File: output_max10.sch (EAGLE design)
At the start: 66 parts, among them IC4 IS61WV1288EEBLL-10HLI, IC5 10M04EQFP144, Q1 25MHz

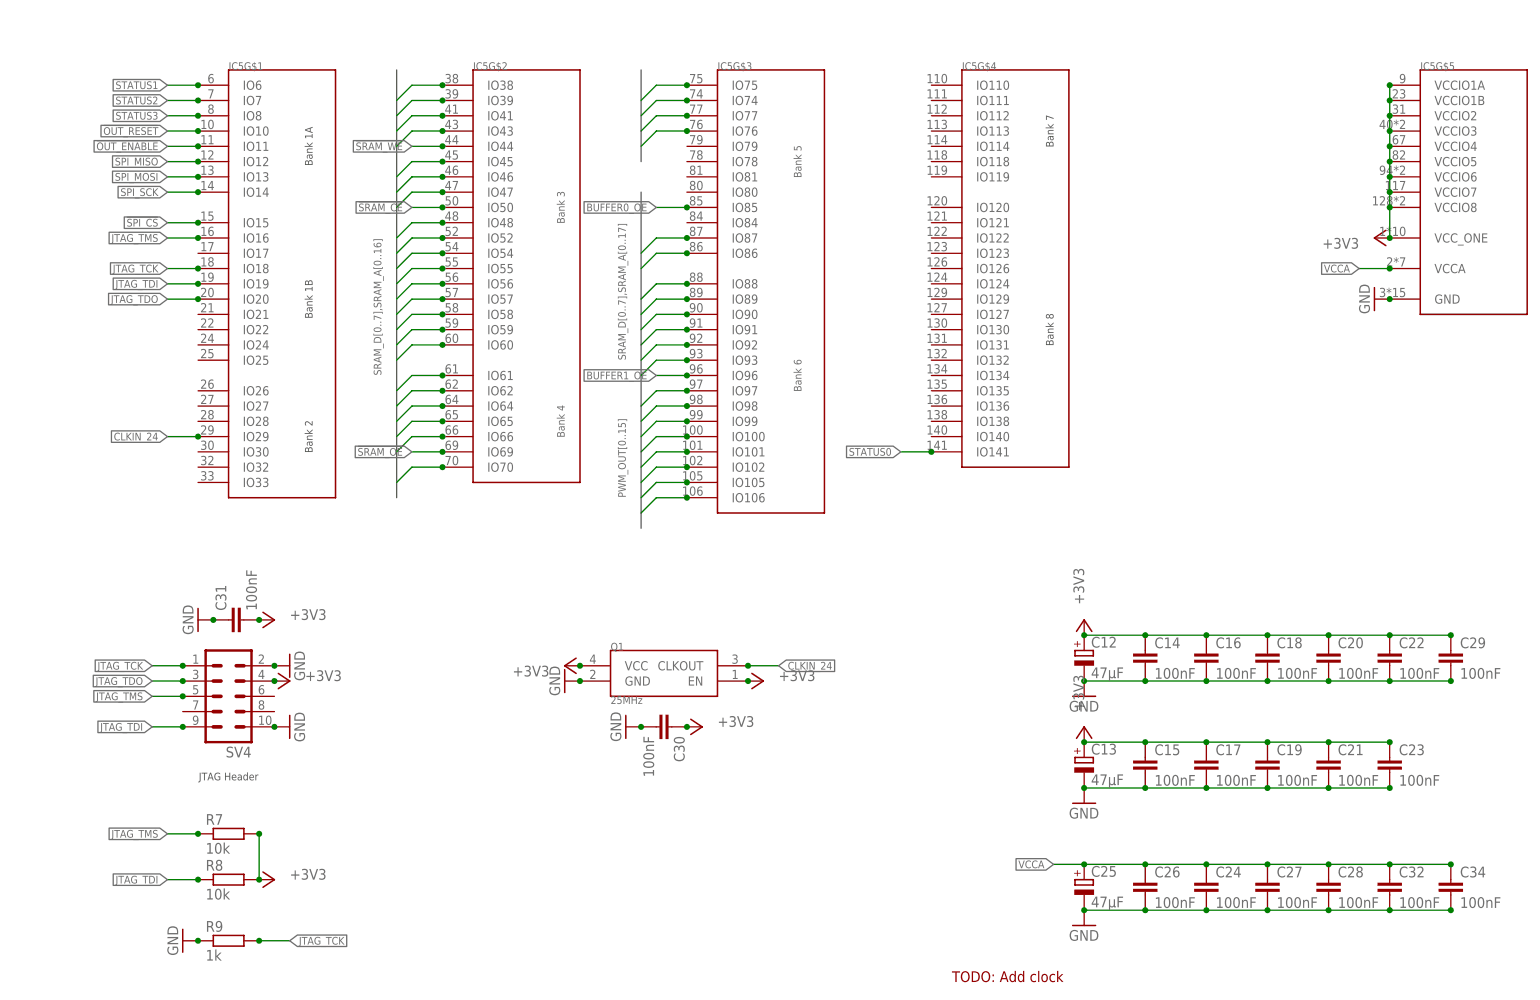
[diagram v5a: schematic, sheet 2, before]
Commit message: Added some required reisstors to FPGA outputboard
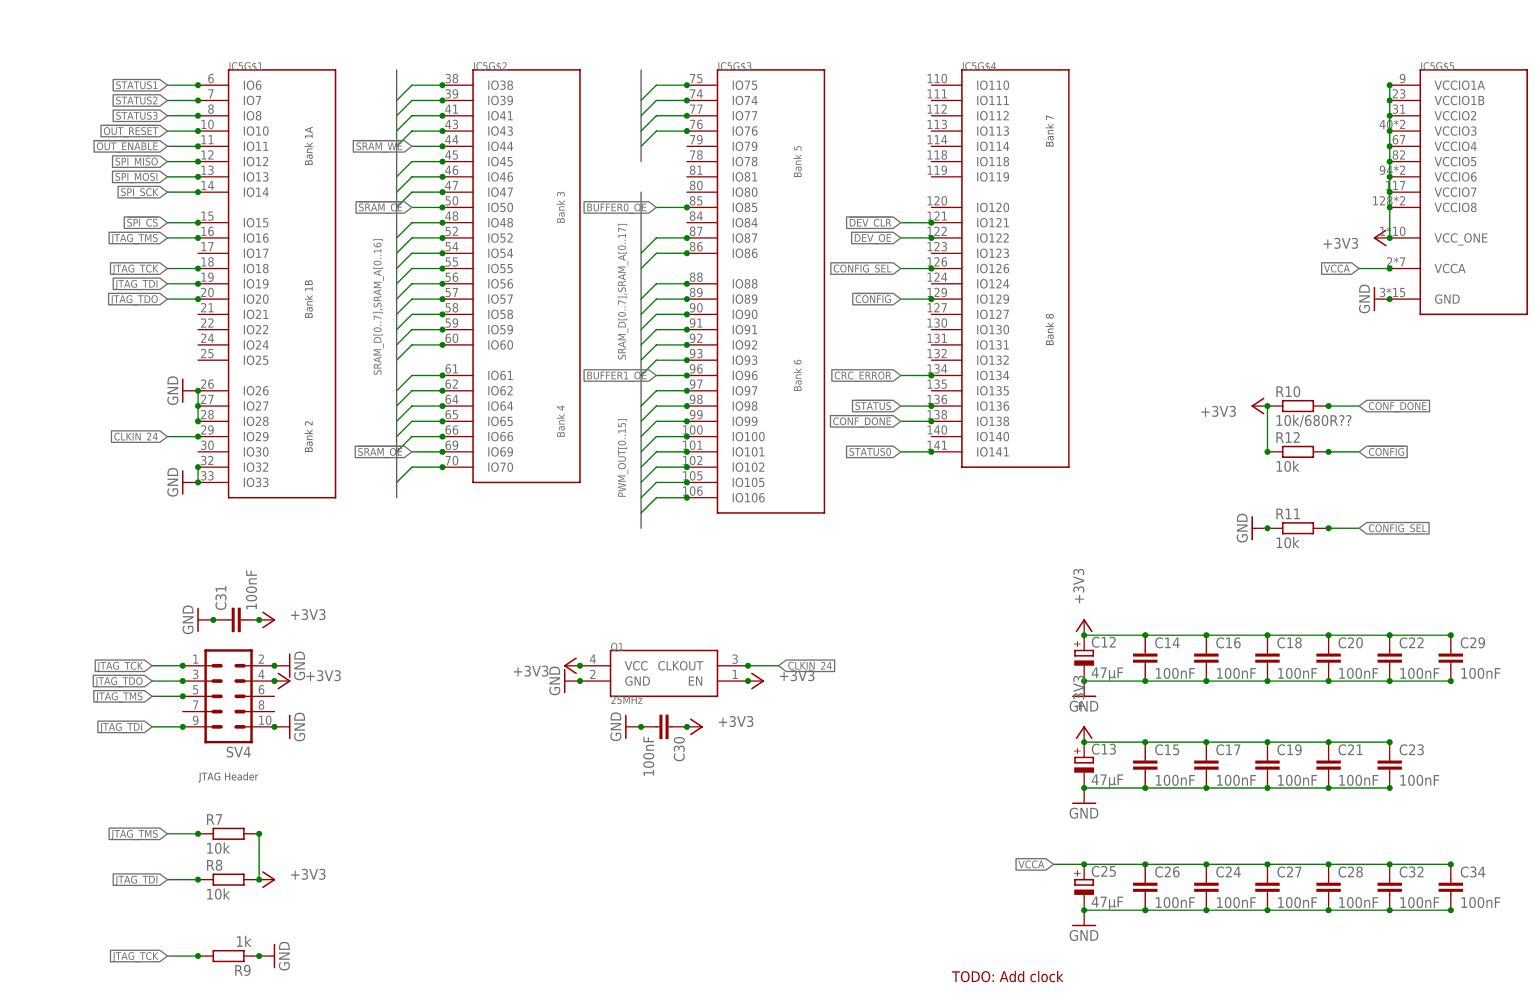
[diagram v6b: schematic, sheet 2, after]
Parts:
- added LED6: (no value), led:LEDCHIPLED_1206
- added R10: 10k/680R??, rcl:R-EU_M0805
- added R11, R12: 10k, rcl:R-EU_M0805
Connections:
- new net !CONFIG: IC5G$4.IO129, R12.2
- new net !DEV_CLR: IC5G$4.IO121
- new net !STATUS: IC5G$4.IO136
- new net CONFIG_SEL: IC5G$4.IO126, R11.2
- new net CONF_DONE: IC5G$4.IO138, LED6.A, R10.2
- new net CRC_ERROR: IC5G$4.IO134
- new net DEV_OE: IC5G$4.IO122
- net +3V3: now also R10.1, R12.1
- net GND: now also IC5G$1.IO26, IC5G$1.IO27, IC5G$1.IO28, IC5G$1.IO32, IC5G$1.IO33, LED6.C, R11.1
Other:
- moved on the sheet: R9
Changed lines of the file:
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@@
 <attribute name="MOUSER" value="710-885012207072"/>
 </part>
+<part name="R10" library="rcl" library_urn="urn:adsk.eagle:library:334" deviceset="R-EU_" device="M0805" package3d_urn="urn:adsk.eagle:package:23556/1" value="10k/680R??">
+<attribute name="MOUSER" value="652-CR0805FX-1002ELF"/>
+</part>
+<part name="+3V10" library="supply1" library_urn="urn:adsk.eagle:library:371" deviceset="+3V3" device=""/>
+<part name="LED6" library="led" library_urn="urn:adsk.eagle:library:259" deviceset="LED" device="CHIPLED_1206" package3d_urn="urn:adsk.eagle:package:15823/2">
+<attribute name="MOUSER" value="604-APTR3216SGC"/>
+</part>
+<part name="R11" library="rcl" library_urn="urn:adsk.eagle:library:334" deviceset="R-EU_" device="M0805" package3d_urn="urn:adsk.eagle:package:23556/1" value="10k">
+<attribute name="MOUSER" value="652-CR0805FX-1002ELF"/>
+</part>
+<part name="GND26" library="supply1" library_urn="urn:adsk.eagle:library:371" deviceset="GND" device=""/>
+<part name="R12" library="rcl" library_urn="urn:adsk.eagle:library:334" deviceset="R-EU_" device="M0805" package3d_urn="urn:adsk.eagle:package:23556/1" value="10k">
+<attribute name="MOUSER" value="652-CR0805FX-1002ELF"/>
+</part>
+<part name="GND27" library="supply1" library_urn="urn:adsk.eagle:library:371" deviceset="GND" device=""/>
+<part name="GND28" library="supply1" library_urn="urn:adsk.eagle:library:371" deviceset="GND" device=""/>
 </parts>
 <sheets>
@@
 <instance part="+3V9" gate="G$1" x="109.22" y="66.04" smashed="yes">
 <attribute name="VALUE" x="109.22" y="66.04" size="1.778" layer="96"/>
+</instance>
+<instance part="LED6" gate="G$1" x="231.14" y="139.7" rot="R90">
+<attribute name="MOUSER" x="231.14" y="139.7" size="1.27" layer="96" rot="R90" align="top-center" display="off"/>
 </instance>
 </instances>
@@
 <wire x1="236.22" y1="154.94" x2="236.22" y2="147.32" width="0.1524" layer="91"/>
 <junction x="236.22" y="147.32"/>
+<pinref part="LED6" gate="G$1" pin="C"/>
+<wire x1="236.22" y1="139.7" x2="236.22" y2="147.32" width="0.1524" layer="91"/>
+<junction x="236.22" y="139.7"/>
 </segment>
 <segment>
@@
 <label x="33.02" y="12.7" size="1.27" layer="95" rot="R270" xref="yes"/>
 <junction x="33.02" y="20.32"/>
+</segment>
+</net>
+<net name="CONF_DONE" class="0">
+<segment>
+<pinref part="LED6" gate="G$1" pin="A"/>
+<wire x1="228.6" y1="139.7" x2="213.36" y2="139.7" width="0.1524" layer="91"/>
+<label x="213.36" y="139.7" size="1.27" layer="95" rot="R180" xref="yes"/>
+<junction x="228.6" y="139.7"/>
 </segment>
 </net>
@@
 <attribute name="MOUSER" x="30.48" y="48.26" size="1.27" layer="96" align="top-center" display="off"/>
 </instance>
-<instance part="R9" gate="G$1" x="30.48" y="38.1">
-<attribute name="MOUSER" x="30.48" y="38.1" size="1.27" layer="96" align="top-center" display="off"/>
-</instance>
-<instance part="GND19" gate="1" x="22.86" y="38.1" rot="R270"/>
+<instance part="R9" gate="G$1" x="30.48" y="35.56" rot="R180">
+<attribute name="MOUSER" x="30.48" y="35.56" size="1.27" layer="96" rot="R180" align="top-center" display="off"/>
+</instance>
+<instance part="GND19" gate="1" x="38.1" y="35.56" rot="R90"/>
 <instance part="+3V2" gate="G$1" x="38.1" y="48.26" smashed="yes" rot="R270">
 <attribute name="VALUE" x="40.64" y="48.26" size="1.778" layer="96"/>
@@
 <attribute name="MOUSER" x="233.68" y="48.26" size="1.27" layer="96" align="top-center" display="off"/>
 </instance>
+<instance part="R10" gate="G$1" x="208.28" y="127">
+<attribute name="MOUSER" x="208.28" y="127" size="1.27" layer="96" align="top-center" display="off"/>
+</instance>
+<instance part="+3V10" gate="G$1" x="200.66" y="127" smashed="yes" rot="R90">
+<attribute name="VALUE" x="198.12" y="127" size="1.778" layer="96" rot="R180"/>
+</instance>
+<instance part="R11" gate="G$1" x="208.28" y="106.68">
+<attribute name="MOUSER" x="208.28" y="106.68" size="1.27" layer="96" align="top-center" display="off"/>
+</instance>
+<instance part="GND26" gate="1" x="200.66" y="106.68" rot="R270"/>
+<instance part="R12" gate="G$1" x="208.28" y="119.38">
+<attribute name="MOUSER" x="208.28" y="119.38" size="1.27" layer="96" align="top-center" display="off"/>
+</instance>
+<instance part="GND27" gate="1" x="22.86" y="129.54" rot="R270"/>
+<instance part="GND28" gate="1" x="22.86" y="114.3" rot="R270"/>
 </instances>
 <busses>
@@
 <junction x="35.56" y="91.44"/>
 </segment>
+<segment>
+<pinref part="R10" gate="G$1" pin="1"/>
+<pinref part="+3V10" gate="G$1" pin="+3V3"/>
+<junction x="203.2" y="127"/>
+<pinref part="R12" gate="G$1" pin="1"/>
+<wire x1="203.2" y1="127" x2="203.2" y2="119.38" width="0.1524" layer="91"/>
+<junction x="203.2" y="119.38"/>
+</segment>
 </net>
 <net name="GND" class="0">
@@
 <pinref part="R9" gate="G$1" pin="1"/>
 <pinref part="GND19" gate="1" pin="GND"/>
-<junction x="25.4" y="38.1"/>
+<junction x="35.56" y="35.56"/>
 </segment>
 <segment>
@@
 <junction x="27.94" y="91.44"/>
 </segment>
+<segment>
+<pinref part="R11" gate="G$1" pin="1"/>
+<pinref part="GND26" gate="1" pin="GND"/>
+<junction x="203.2" y="106.68"/>
+</segment>
+<segment>
+<pinref part="IC5" gate="G$1" pin="IO26"/>
+<pinref part="IC5" gate="G$1" pin="IO28"/>
+<wire x1="25.4" y1="129.54" x2="25.4" y2="127" width="0.1524" layer="91"/>
+<junction x="25.4" y="129.54"/>
+<pinref part="IC5" gate="G$1" pin="IO27"/>
+<junction x="25.4" y="127"/>
+<wire x1="25.4" y1="127" x2="25.4" y2="124.46" width="0.1524" layer="91"/>
+<junction x="25.4" y="124.46"/>
+<pinref part="GND27" gate="1" pin="GND"/>
+</segment>
+<segment>
+<pinref part="IC5" gate="G$1" pin="IO32"/>
+<pinref part="IC5" gate="G$1" pin="IO33"/>
+<wire x1="25.4" y1="116.84" x2="25.4" y2="114.3" width="0.1524" layer="91"/>
+<junction x="25.4" y="116.84"/>
+<junction x="25.4" y="114.3"/>
+<pinref part="GND28" gate="1" pin="GND"/>
+</segment>
 </net>
 <net name="JTAG_TMS" class="0">
@@
 <segment>
 <pinref part="R9" gate="G$1" pin="2"/>
-<wire x1="35.56" y1="38.1" x2="40.64" y2="38.1" width="0.1524" layer="91"/>
-<label x="40.64" y="38.1" size="1.27" layer="95" xref="yes"/>
-<junction x="35.56" y="38.1"/>
+<wire x1="25.4" y1="35.56" x2="20.32" y2="35.56" width="0.1524" layer="91"/>
+<label x="20.32" y="35.56" size="1.27" layer="95" rot="R180" xref="yes"/>
+<junction x="25.4" y="35.56"/>
 </segment>
 </net>
@@
 </segment>
 </net>
+<net name="CONF_DONE" class="0">
+<segment>
+<pinref part="IC5" gate="G$4" pin="IO138"/>
+<wire x1="147.32" y1="124.46" x2="142.24" y2="124.46" width="0.1524" layer="91"/>
+<label x="142.24" y="124.46" size="1.27" layer="95" rot="R180" xref="yes"/>
+<junction x="147.32" y="124.46"/>
+</segment>
+<segment>
+<pinref part="R10" gate="G$1" pin="2"/>
+<wire x1="213.36" y1="127" x2="218.44" y2="127" width="0.1524" layer="91"/>
+<label x="218.44" y="127" size="1.27" layer="95" xref="yes"/>
+<junction x="213.36" y="127"/>
+</segment>
+</net>
+<net name="!STATUS" class="0">
+<segment>
+<pinref part="IC5" gate="G$4" pin="IO136"/>
+<wire x1="147.32" y1="127" x2="142.24" y2="127" width="0.1524" layer="91"/>
+<label x="142.24" y="127" size="1.27" layer="95" rot="R180" xref="yes"/>
+<junction x="147.32" y="127"/>
+</segment>
+</net>
+<net name="CONFIG_SEL" class="0">
+<segment>
+<pinref part="IC5" gate="G$4" pin="IO126"/>
+<wire x1="147.32" y1="149.86" x2="142.24" y2="149.86" width="0.1524" layer="91"/>
+<label x="142.24" y="149.86" size="1.27" layer="95" rot="R180" xref="yes"/>
+<junction x="147.32" y="149.86"/>
+</segment>
+<segment>
+<pinref part="R11" gate="G$1" pin="2"/>
+<wire x1="213.36" y1="106.68" x2="218.44" y2="106.68" width="0.1524" layer="91"/>
+<label x="218.44" y="106.68" size="1.27" layer="95" xref="yes"/>
+<junction x="213.36" y="106.68"/>
+</segment>
+</net>
+<net name="CRC_ERROR" class="0">
+<segment>
+<pinref part="IC5" gate="G$4" pin="IO134"/>
+<wire x1="147.32" y1="132.08" x2="142.24" y2="132.08" width="0.1524" layer="91"/>
+<label x="142.24" y="132.08" size="1.27" layer="95" rot="R180" xref="yes"/>
+<junction x="147.32" y="132.08"/>
+</segment>
+</net>
+<net name="DEV_OE" class="0">
+<segment>
+<pinref part="IC5" gate="G$4" pin="IO122"/>
+<wire x1="147.32" y1="154.94" x2="142.24" y2="154.94" width="0.1524" layer="91"/>
+<label x="142.24" y="154.94" size="1.27" layer="95" rot="R180" xref="yes"/>
+<junction x="147.32" y="154.94"/>
+</segment>
+</net>
+<net name="!DEV_CLR" class="0">
+<segment>
+<pinref part="IC5" gate="G$4" pin="IO121"/>
+<wire x1="147.32" y1="157.48" x2="142.24" y2="157.48" width="0.1524" layer="91"/>
+<label x="142.24" y="157.48" size="1.27" layer="95" rot="R180" xref="yes"/>
+<junction x="147.32" y="157.48"/>
+</segment>
+</net>
+<net name="!CONFIG" class="0">
+<segment>
+<pinref part="IC5" gate="G$4" pin="IO129"/>
+<wire x1="147.32" y1="144.78" x2="142.24" y2="144.78" width="0.1524" layer="91"/>
+<label x="142.24" y="144.78" size="1.27" layer="95" rot="R180" xref="yes"/>
+<junction x="147.32" y="144.78"/>
+</segment>
+<segment>
+<pinref part="R12" gate="G$1" pin="2"/>
+<wire x1="213.36" y1="119.38" x2="218.44" y2="119.38" width="0.1524" layer="91"/>
+<label x="218.44" y="119.38" size="1.27" layer="95" xref="yes"/>
+<junction x="213.36" y="119.38"/>
+</segment>
+</net>

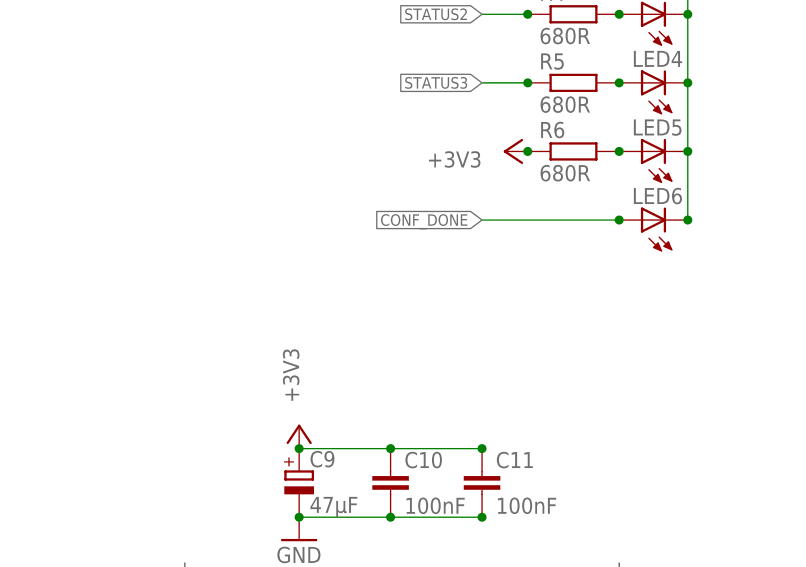
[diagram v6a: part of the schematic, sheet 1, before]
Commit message: Minor component placemnet changes for MAX10 output board to fix mechanical issues
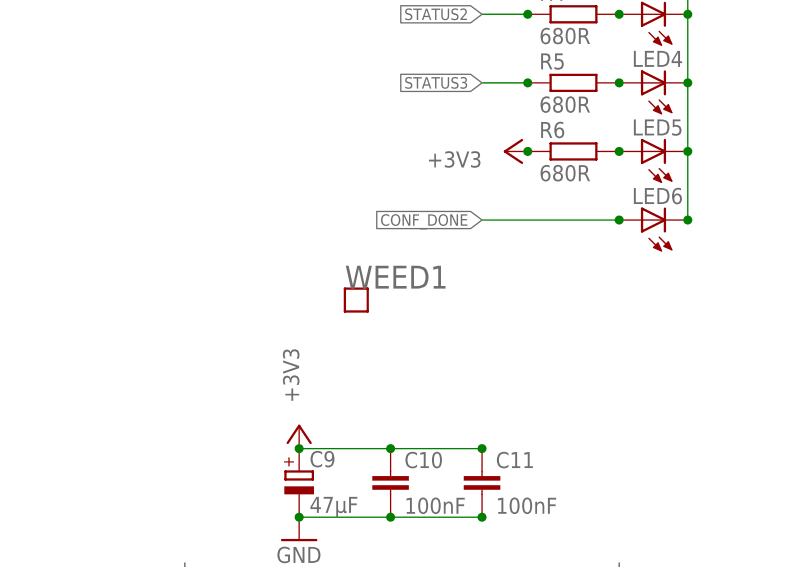
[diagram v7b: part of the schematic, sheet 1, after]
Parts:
- added WEED1: WEED, lichtenstein_onion:WEED
- R10: value 10k/680R?? -> 10k
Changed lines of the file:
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@@
 <attribute name="MOUSER" value="710-885012207072"/>
 </part>
-<part name="R10" library="rcl" library_urn="urn:adsk.eagle:library:334" deviceset="R-EU_" device="M0805" package3d_urn="urn:adsk.eagle:package:23556/1" value="10k/680R??">
+<part name="R10" library="rcl" library_urn="urn:adsk.eagle:library:334" deviceset="R-EU_" device="M0805" package3d_urn="urn:adsk.eagle:package:23556/1" value="10k">
 <attribute name="MOUSER" value="652-CR0805FX-1002ELF"/>
 </part>
@@
 <part name="GND27" library="supply1" library_urn="urn:adsk.eagle:library:371" deviceset="GND" device=""/>
 <part name="GND28" library="supply1" library_urn="urn:adsk.eagle:library:371" deviceset="GND" device=""/>
+<part name="WEED1" library="lichtenstein_onion" deviceset="WEED" device=""/>
 </parts>
 <sheets>
@@
 <attribute name="MOUSER" x="231.14" y="139.7" size="1.27" layer="96" rot="R90" align="top-center" display="off"/>
 </instance>
+<instance part="WEED1" gate="G$1" x="198.12" y="129.54"/>
 </instances>
 <busses>
